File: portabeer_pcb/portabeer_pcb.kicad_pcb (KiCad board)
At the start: 2 copper layers, 100 x 100 mm, 292 parts, among them J1 USB_B_Micro, J10 Conn_01x03, J11 Conn_01x03, J12 Conn_01x03, J13 XT60IPW, J14 Barrel_Jack_MountingPin, J15 Conn_01x03, J16 Conn_01x03, J17 Conn_01x03, J19 FAN, J2 GMG12864-06D, J20 FAN, J21 WATER PUMP, J22 WATER PUMP, J3 Conn_01x03, J4 Conn_01x08, J5 Conn_01x03, J6 Conn_01x03, J7 Conn_01x03, J8 Conn_01x03, J9 Conn_01x03, M1 Air pump, Q1 AO3400A, Q10 AO3400A, Q11 AO3400A, Q12 Si7336ADP, Q13 Si7336ADP, Q14 AO3400A, Q16 Si7336ADP, Q17 Si7336ADP, Q2 BSS84, Q3 BSS138, Q4 Si7145DP, Q5 Si7145DP, Q6 SiS454DN, Q7 AO3400A, Q8 AO3400A, SW1 RESET, SW2 BOOTSEL, SW3 RotaryEncoder_Switch_MP, U1 USBLC6-2SC6, U10 LTC4412xS6, U11 MP26124, U12 PCA9536DP, U14 TPS92640PWP/NOPB, U15 TPS92640PWP/NOPB, U16 MCP47FEB12, U17 REF3012, U2 W25Q128JVS, U3 RP2040, U4 COS1416, U5 XC6206PxxxMR, U6 TPS54202DDC, U7 LTC2954-1, U8 ADS7828, U9 LTC2943, Y1 Crystal_GND24

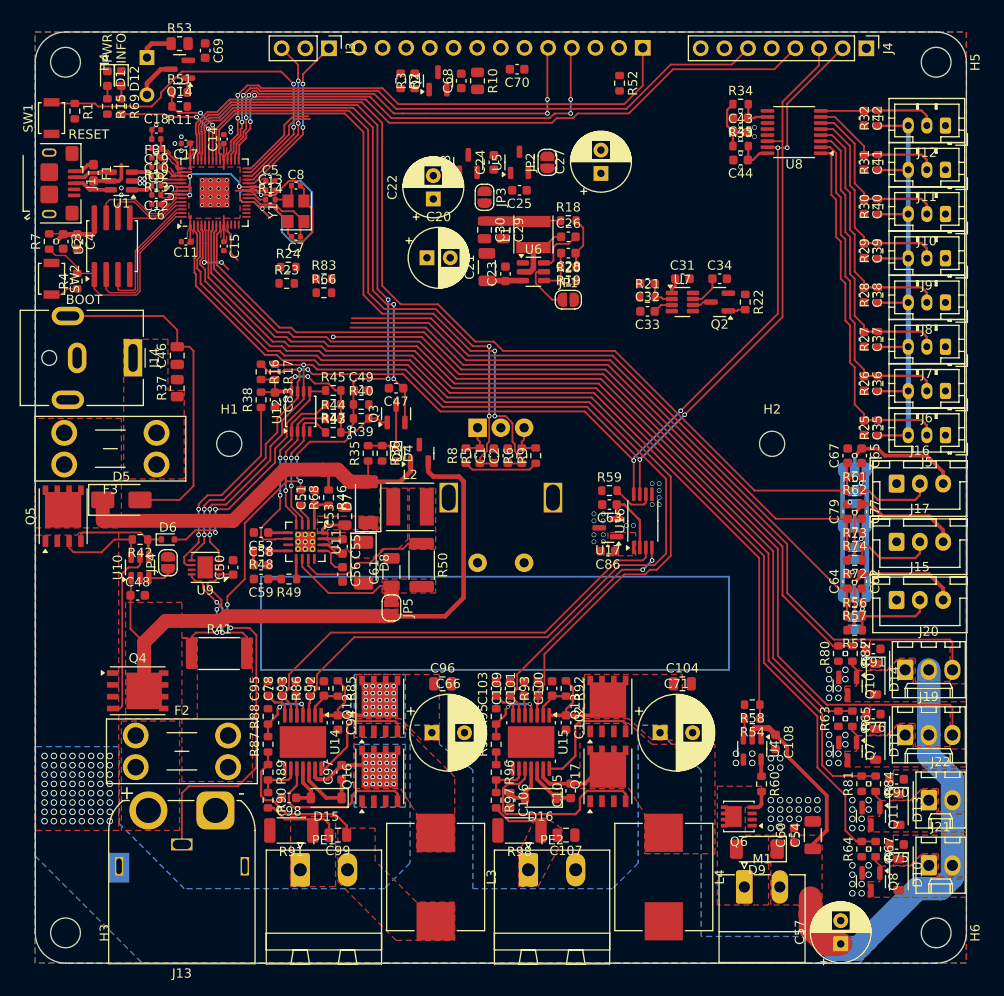
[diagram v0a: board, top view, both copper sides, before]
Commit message: added capacitive sensor
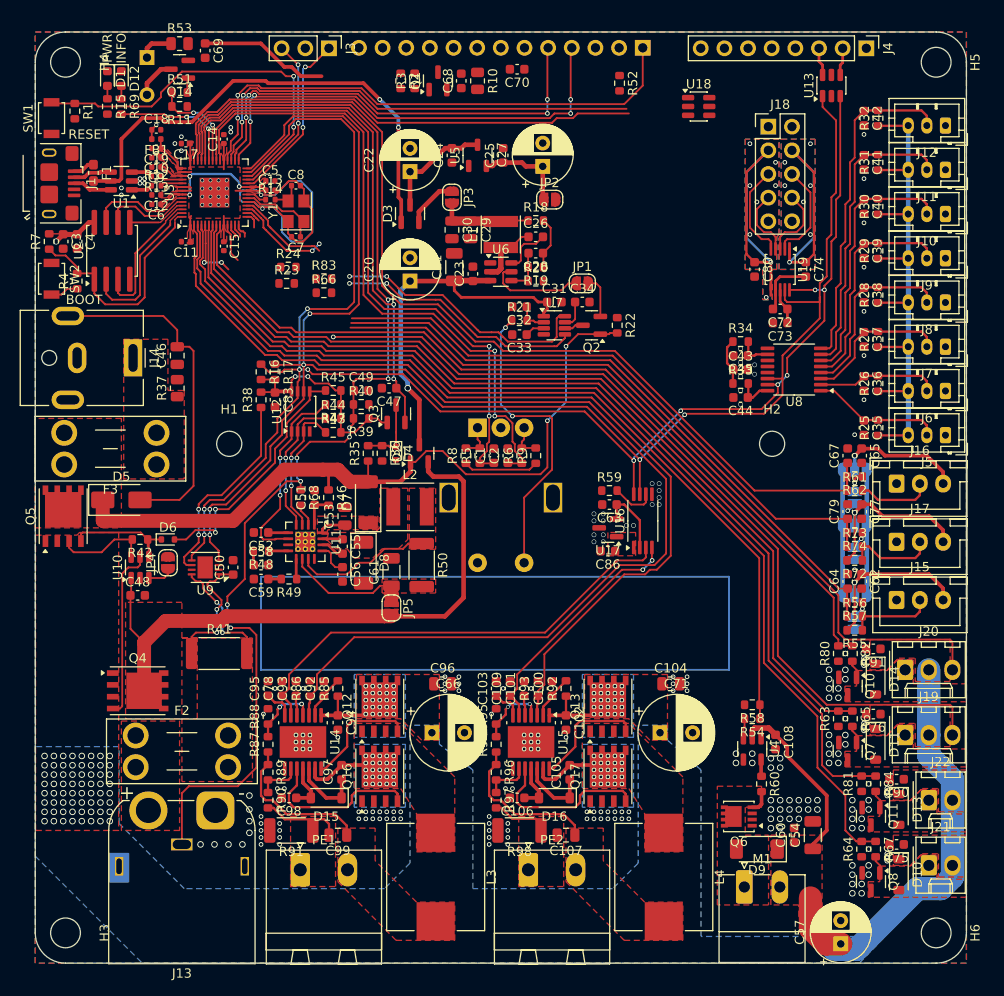
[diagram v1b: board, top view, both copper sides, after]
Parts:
- added C72: 100n, Capacitor_SMD:C_0603_1608Metric, F.Cu at (255.5, 59.0)
- added C73: 1u, Capacitor_SMD:C_0603_1608Metric, F.Cu at (255.5, 60.5)
- added C74: C, Capacitor_SMD:C_0603_1608Metric, F.Cu at (258.2, 54.8)
- added C80: C, Capacitor_SMD:C_0603_1608Metric, F.Cu at (252.8, 54.8)
- added J18: Conn_02x05_Odd_Even, Connector_PinHeader_2.54mm:PinHeader_2x05_P2.54mm_Vertical, F.Cu at (254.2, 39.4)
- added U13: USBLC6-2SC6, Package_TO_SOT_SMD:SOT-23-6, F.Cu at (261.0, 35.0)
- added U18: USBLC6-4SC6, Package_TO_SOT_SMD:SOT-23-6, F.Cu at (246.8, 37.2)
- added U19: FDC1004DGST, Package_SO:VSSOP-10_3x3mm_P0.5mm, F.Cu at (255.5, 54.8)
- moved C43 25.5 mm to (251.2, 65.5)
- moved C44 25.5 mm to (251.2, 68.5)
- moved C45 25.5 mm to (251.2, 64.0)
- moved R33 25.5 mm to (251.2, 67.0)
- moved R34 25.5 mm to (251.2, 62.5)
- moved U8 25.5 mm to (257.0, 65.5)
- moved C34 15.0 mm to (234.2, 58.2)
- moved C31 14.0 mm to (231.2, 58.2)
- moved C32 14.0 mm to (227.5, 58.8)
- moved C33 14.0 mm to (227.5, 61.8)
- moved Q2 14.0 mm to (235.2, 60.8)
- moved R21 14.0 mm to (227.5, 60.2)
- moved R22 14.0 mm to (238.0, 60.8)
- moved U7 14.0 mm to (231.2, 60.8)
- moved D3 8.24 mm to (215.8, 48.8)
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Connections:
- net Net-(JP2-A) renamed /PWR/3V3_OUT
- net Net-(JP3-B) renamed /PWR/5V_OUT
- net Net-(U6-BOOT) renamed /PWR/5V_BST
- net Net-(U6-SW) renamed /PWR/5V_SW
- C22 pad 1: /PWR/VR_{SEC} -> +5V
- C24 pad 2: /PWR/VR_{SEC} -> +5V
- D3 pad 2: +5V -> /PWR/VR_{SEC}
- D3 pad 3: /PWR/VR_{SEC} -> +5V
- J4 pad 2: /SDA -> /EXP/ESDA
- J4 pad 3: /SCL -> /EXP/ESCL
- JP3 pad 1: +5V -> /PWR/VR_{SEC}
- U5 pad 3: /PWR/VR_{SEC} -> +5V
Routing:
- net VBUS: track 4.60 -> 53.0 mm, vias 0 -> 2
- net /SCL: track 136.9 -> 179.5 mm, vias 5 -> 6
- net /SDA: track 139.3 -> 178.0 mm, vias 8 -> 11
- net /PWR/VR_{PRI}: track 5.59 -> 40.9 mm, vias 0 -> 1
- net VDC: track 46.1 -> 80.7 mm, vias 0 -> 2
- net /~{PB}: track 0.00 -> 32.4 mm, vias 0 -> 2
- net /EXP/SHLD2: track 0.00 -> 32.2 mm, vias 0 -> 8
- net /EXP/SHLD1: track 0.00 -> 30.6 mm, vias 0 -> 7
- net /~{KILL}: track 4.27 -> 32.6 mm, vias 0 -> 2
- net /~{INT}: track 0.00 -> 28.2 mm, vias 0 -> 2
- net +5V: track 13.5 -> 39.5 mm
- net /ADC/CH0: track 39.2 -> 14.0 mm
- net /ADC/CH7: track 12.7 -> 35.9 mm
- net /ADC/CH1: track 35.2 -> 13.0 mm
- net /IO29: track 73.9 -> 53.2 mm
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- added copper zone on B.Cu, net /EXP/SHLD1
- added copper zone on F.Cu, net /EXP/SHLD1
- added copper zone on B.Cu, net /EXP/SHLD2
- added copper zone on F.Cu, net /EXP/SHLD2
- added copper zone on F.Cu, net /KEG2/Driver/OUT+
- added copper zone on B.Cu, net /KEG2/Driver/SW

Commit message: layout
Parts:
- removed H1, H2: MountingHole, MountingHole:MountingHole_2.7mm_M2.5
- removed H3, H4, H5, H6: MountingHole, MountingHole:MountingHole_3.2mm_M3
- removed U18: USBLC6-4SC6, Package_TO_SOT_SMD:SOT-23-6
- added C81: 100n, Capacitor_SMD:C_0603_1608Metric, F.Cu at (130.8, 43.0)
- added C84: 100n, Capacitor_SMD:C_0603_1608Metric, F.Cu at (120.5, 42.0)
- added D17: MBR0530, Diode_SMD:D_SOD-123, F.Cu at (117.2, 41.8)
- added H10: MountingHole_Pad, MountingHole:MountingHole_3.2mm_M3_Pad, F.Cu at (143.5, 40.5)
- added H11: MountingHole_Pad, MountingHole:MountingHole_3.2mm_M3_Pad, F.Cu at (143.5, 134.0)
- added H12: MountingHole_Pad, MountingHole:MountingHole_3.2mm_M3_Pad, F.Cu at (50.0, 134.0)
- added H7: MountingHole_Pad, MountingHole:MountingHole_2.7mm_M2.5_Pad, F.Cu at (67.6, 81.5)
- added H8: MountingHole_Pad, MountingHole:MountingHole_2.7mm_M2.5_Pad, F.Cu at (125.9, 81.5)
- added H9: MountingHole_Pad, MountingHole:MountingHole_3.2mm_M3_Pad, F.Cu at (50.0, 40.5)
- added J23: Conn_01x02, Connector_PinHeader_2.54mm:PinHeader_1x02_P2.54mm_Vertical, F.Cu at (112.0, 49.0)
- added J24: Conn_01x04, Connector_PinHeader_2.54mm:PinHeader_1x04_P2.54mm_Vertical, F.Cu at (138.1, 39.0)
- added Q9: AO3400A, Package_TO_SOT_SMD:SOT-23, F.Cu at (116.5, 44.8)
- added R70: 10k, Resistor_SMD:R_0603_1608Metric, F.Cu at (96.8, 98.2)
- added R71: 100k, Resistor_SMD:R_0603_1608Metric, F.Cu at (120.0, 44.2)
- added R75: 10, Resistor_SMD:R_0603_1608Metric, F.Cu at (120.0, 45.8)
- added TH1: Thermistor_NTC, Resistor_SMD:R_0603_1608Metric_Pad0.98x0.95mm_HandSolder, F.Cu at (96.8, 101.5)
- J14: moved to B.Cu
- J4: value Conn_01x08 -> Conn_01x02; footprint Connector_PinHeader_2.54mm:PinHeader_1x08_P2.54mm_Vertical -> Connector_JST:JST_XH_S2B-XH-A_1x02_P2.50mm_Horizontal; moved to B.Cu
- moved J4 145.7 mm to (119.2, 39.2), turned to 180 degrees
- moved R52 129.7 mm to (108.8, 41.2), turned to 180 degrees
- moved JP1 129.5 mm to (104.8, 58.5)
- moved BZ1 129.0 mm to (58.8, 40.0)
- moved C1 129.0 mm to (96.0, 82.8)
- moved C10 129.0 mm to (59.8, 50.8)
- moved C100 129.0 mm to (102.2, 107.8)
- moved C101 129.0 mm to (99.2, 107.8)
- moved C102 129.0 mm to (103.7, 111.4)
- moved C103 129.0 mm to (96.2, 107.8)
- moved C104 129.0 mm to (115.0, 107.2)
- moved C105 129.0 mm to (104.2, 116.8)
- moved C106 129.0 mm to (98.5, 119.5)
- moved C107 129.0 mm to (103.8, 123.5)
- moved C108 129.0 mm to (126.2, 113.5)
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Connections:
- J4 pad 1: GND -> VCC
- J4 pad 2: /EXP/ESDA -> /EXP/FAN
- U13 pad 5: +5V -> +3.3V
- U3 pad 31: /IO20 -> /PCB_FAN
- U3 pad 41: /IO29 -> /MCU/PCB_NTC
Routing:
- net +3.3V: track 160.4 -> 408.3 mm, vias 5 -> 19
- net +5V: track 39.5 -> 146.8 mm, vias 0 -> 3
- net /MCU/PCB_NTC: track 0.00 -> 99.1 mm, vias 0 -> 2
- net VCC: track 96.0 -> 189.9 mm
- net /PCB_FAN: track 0.00 -> 63.8 mm, vias 0 -> 2
- net /IO29: track 53.2 -> 0.00 mm
- net /IO20: track 50.0 -> 0.00 mm, vias 2 -> 0
- net /MCU/LCD_DC: track 10.4 -> 56.3 mm, vias 2 -> 4
- net /~{INT}: track 28.2 -> 66.5 mm, vias 2 -> 4
- net /MCU/LCD_BL: track 7.06 -> 40.4 mm, vias 2 -> 6
- net /~{KILL}: track 32.6 -> 65.1 mm, vias 2 -> 4
- net /~{ALCC}: track 23.6 -> 44.7 mm, vias 2 -> 4
- net VDC: track 80.7 -> 101.1 mm
- net /FAN_TACH_1: track 94.3 -> 114.1 mm, vias 1 -> 2
- net /FLOW_1: track 69.6 -> 89.1 mm
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- added copper zone on F.Cu, net /EXP/FAN
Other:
- board text added: "+ -"
- board text added: "+ s -"
- board text added: "- +"
- board text added: "- s +"
- board text added: "3V"
- board text added: "3V3 SCL SDA GND"
- board text added: "5V"
- board text added: "A0"
- board text added: "A1"
- board text added: "A2"
- board text added: "A3"
- board text added: "A4"
- board text added: "A5"
- board text added: "A6"
- board text added: "A7"
- board text added: "AP"
- board text added: "BATTERY"
- board text added: "BLK BLA GND 3V3 MOSI SCK DC RSTn CS"
- board text added: "DC IN 20V"
- board text added: "FAN1"
- board text added: "FAN2"
- board text added: "FS1"
- board text added: "FS2"
- board text added: "GND SH1 CI1 CI2 SH1"
- board text added: "GND SH2 CI4 CI3 SH2"
- board text added: "NTC"
- board text added: "PS"
- board text added: "REG IN"
- board text added: "REG OUT"
- board text added: "SWD GND SWC"
- board text added: "TEC1"
- board text added: "TEC2"
- board text added: "WP1"
- board text added: "WP2"
- board text added: "s + -"
